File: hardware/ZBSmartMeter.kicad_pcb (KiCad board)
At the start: 2 copper layers, 43.3 x 37.6 mm, 37 parts, among them J1 RJ12, J2 Conn_01x04, J3 Conn_01x02, J5 Screw_Terminal_01x02, J6 USB_C_Receptacle_USB2.0, SW1 SW_Push, SW2 SW_Push, U1 NCN5150DG, U2 TLV1117-33, U3 ESP32-C6-MINI-1/U

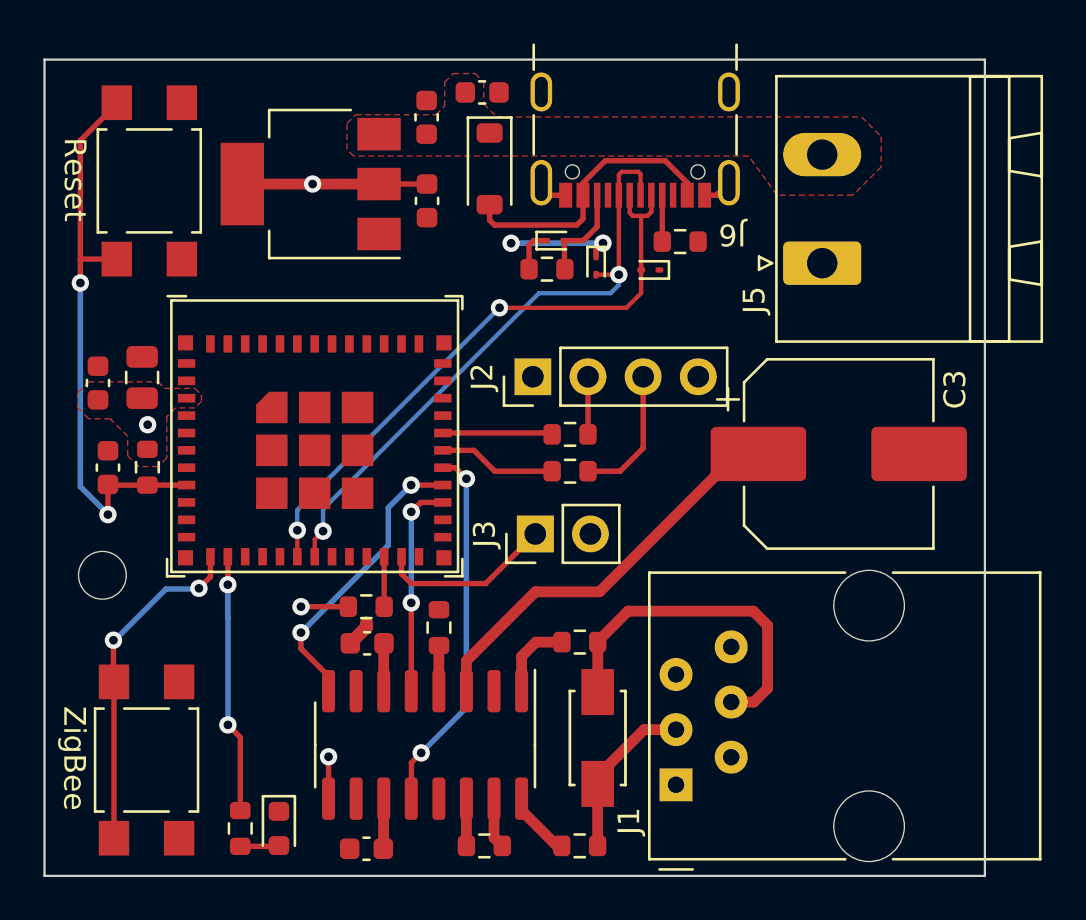
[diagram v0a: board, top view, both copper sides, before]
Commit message: fixed diode error, improved layout
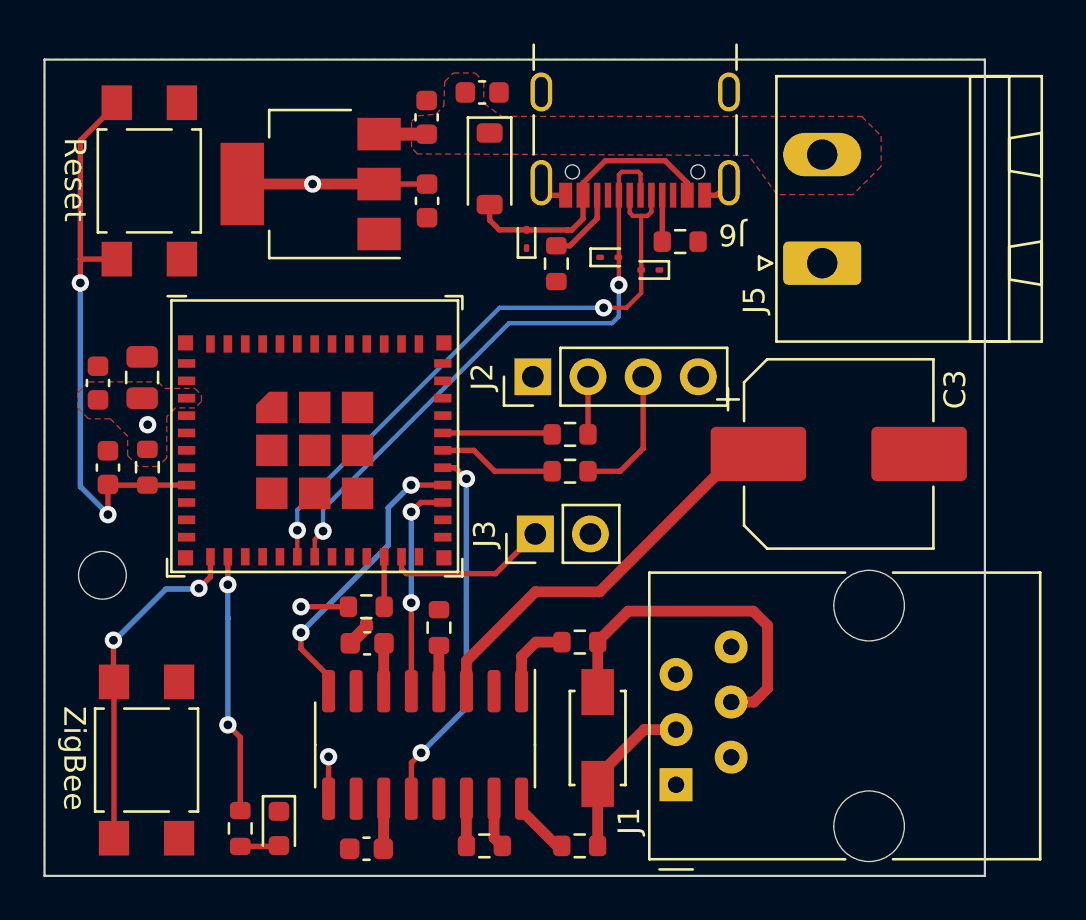
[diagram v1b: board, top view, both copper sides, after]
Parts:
- moved D6 1.32 mm to (183.9, 91.3), turned to 90 degrees
- moved D4 0.71 mm to (187.7, 92.2), turned to 0 degrees
- moved R11 0.50 mm to (185.2, 92.5), turned to 90 degrees
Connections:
- D6 pad 2: Net-(D6-A2) -> Net-(D3-A)
- J6 pad B5: Net-(D6-A2) -> Net-(J6-CC2)
- R11 pad 2: Net-(D6-A2) -> Net-(J6-CC2)
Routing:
- net GND: track 13.6 -> 6.63 mm, vias 2 -> 0
- net Net-(D6-A2): track 4.55 -> 0.00 mm
- net Net-(J6-CC2): track 0.00 -> 3.47 mm
- net +5V: track 0.00 -> 2.19 mm
- net GPIO9_BOOT_OPTION: track 8.08 -> 7.57 mm
